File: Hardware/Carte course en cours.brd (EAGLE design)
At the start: 160 x 100 mm, 43 parts, among them J1 AVR_SPI_PROG_3X2NS, J3 PWR IN, J4 RC receiver, J5 ESC, J6 MICRO-SD_CARD_SOCKET, U1 V_REG_317DPACK, U2 ATMEGA328P_TQFP, U3 V_REG_317SMD, U4 FT232RL, U5 TXB0104, U6 MPU6050, Y1 16MHz

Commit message: Place components
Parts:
- removed C13: 100n, rcl:C0805
- removed C14: 2.2n, rcl:C0805
- removed C15: 10n, rcl:C0805
- removed R13: 100k, rcl:R0805
- removed U5: TXB0104, SparkFun-IC-Comms:TSSOP14
- removed U6: MPU6050, invensense:HVQFN24_NS
- added J7: MICRO-SD_CARD_SOCKET, SparkFun-Connectors:MICRO-SD-SOCKET
- added J8: ESC, SparkFun-Connectors:1X02
- C1: value 4.7u -> 22p
- C11: value 100n -> 2.2n
- C12: value 100n -> 10n
- C3: value 22p -> 100n
- C4: value 1u -> 100n
- C6: value 100n -> 4.7u
- C8: value 4.7u -> 100n
- J1: value AVR_SPI_PROG_3X2NS -> (none); device SparkFun-Connectors:2X3-NS -> SparkFun-Connectors:USB-B-MICRO-SMD
- J2: value (none) -> AVR_SPI_PROG_3X2NS; device SparkFun-Connectors:USB-B-MICRO-SMD -> SparkFun-Connectors:2X3-NS
- J6: value MICRO-SD_CARD_SOCKET -> ESC; device SparkFun-Connectors:MICRO-SD-SOCKET -> SparkFun-Connectors:1X02
- R1: value 3k -> 10k
- R2: value 10k -> 1.6k
- R4: value 1.6k -> 330
- R5: value 1k -> 330
- R6, R7: value 330 -> 100k
- U1: value V_REG_317DPACK -> V_REG_317SMD; device SparkFun-IC-Power:V-REG_DPACK -> SparkFun-IC-Power:SOT223
- U3: value V_REG_317SMD -> FT232RL; device SparkFun-IC-Power:SOT223 -> SparkFun-IC-Comms:SSOP28DB
- U4: value FT232RL -> MPU6050; device SparkFun-IC-Comms:SSOP28DB -> invensense:HVQFN24_NS
- moved J4 103.9 mm to (44.5, 14.0), turned to 90 degrees
- moved R8 96.1 mm to (33.7, 4.45), flipped to the bottom, turned to 270 degrees
- moved C2 94.8 mm to (26.7, 21.6), flipped to the bottom
- moved R9 92.0 mm to (35.6, 4.45), flipped to the bottom, turned to 270 degrees
- moved U2 87.8 mm to (34.3, 13.3), flipped to the bottom, turned to 180 degrees
- moved LED2 81.3 mm to (17.8, 3.17)
- moved C3 80.5 mm to (21.6, 22.2), turned to 270 degrees
- moved LED1 79.9 mm to (21.0, 3.17)
- moved C8 79.3 mm to (23.5, 3.17), turned to 90 degrees
- moved C9 73.0 mm to (16.5, 14.6), flipped to the bottom, turned to 180 degrees
- moved Y1 72.0 mm to (26.7, 17.1), flipped to the bottom, turned to 270 degrees
- moved R12 71.9 mm to (26.7, 22.2), turned to 270 degrees
- moved R10 71.9 mm to (41.3, 9.53), turned to 270 degrees
- moved J5 71.1 mm to (1.91, 17.8), turned to 90 degrees
- moved R2 67.9 mm to (12.7, 22.2), turned to 180 degrees
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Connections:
- removed net N$11: J6.CS, R10.1, U5.13
- removed net N$17: J6.DI, U5.12
- removed net N$19: J6.SCLK, U5.11
- removed net N$20: J6.DO, U5.10
- removed net N$3: R4.2, R5.2, U3.1
- removed net RXFTDI: U2.31, U4.5
- removed net TXFTDI: U2.30, U4.1
- removed net VCC: C1.2, J3.2, U1.3
- new net RX_AVR: R7.2, U2.30, U3.1
- new net RX_ESP: J5.2, R6.1
- new net TX_AVR: R6.2, U2.31, U3.5
- new net TX_ESP: J8.1, R7.1
- net +3V3: now also C3.2, C4.2, C5.2, C6.2, C8.1, C9.1, J2.2, J3.2, J7.VCC, J8.2, LED1.A, LED2.A, R1.2, R10.1, R12.1, R3.1, U1.2, U2.18, U2.4, U2.6, U3.20, U3.4, U4.13; no longer C11.1, C12.1, J6.VCC, R10.2, R13.1, R5.1, U3.2, U5.14, U6.13
- net +5V: now also J1.VBUS, U1.3; no longer C10.1, C4.1, C5.2, C6.2, C8.2, C9.2, J1.2, J2.VBUS, LED1.A, LED2.A, R12.1, R2.2, R3.1, U1.4, U2.18, U2.4, U2.6, U3.3, U4.20, U4.4, U5.1
- net CARDDETECT: now also J7.CD2; no longer J6.CD2
- net CS: now also J7.CS; no longer U5.2
- net ESC_OUT: now also J6.2; no longer J5.2
- net GND: now also C1.2, C3.1, C4.1, C8.2, C9.2, J1.GND, J2.6, J6.1, J7.GND, J7.GND1, J7.GND3, R2.1, U3.18, U3.21, U3.25, U3.26, U3.7, U4.1, U4.11, U4.9; no longer C1.1, C13.2, C14.2, C15.2, C3.2, C4.2, C8.1, C9.1, J1.6, J2.GND, J6.GND, J6.GND1, J6.GND3, R1.1, R4.1, U4.21, U4.25, U4.26, U4.7, U5.7, U6.1, U6.11, U6.18, U6.9
- net INT: now also U4.12; no longer U6.12
- net MISO: now also J2.1, J7.DO; no longer J1.1, U5.5
- net MOSI: now also J2.4, J7.DI; no longer J1.4, U5.3
- net N$1: now also R2.2; no longer R1.2
- net N$10: now also C11.1, U4.20; no longer C14.1, U6.20
- net N$12: now also R4.1, U3.23; no longer R6.1, U4.23
- net N$13: now also R5.1, U3.22; no longer R7.1, U4.22
- net N$14: now also R4.2; no longer R6.2
- net N$15: now also R5.2; no longer R7.2
- net N$16: now also C10.1, U4.10; no longer C13.1, U6.10
- net N$18: now also C12.1, U4.8; no longer C15.1, U6.8
- net N$2: now also J1.D-, U3.16; no longer J2.D-, U4.16
- net N$27: now also J7.RSV1, R10.2; no longer J6.RSV1, R11.2
- net N$28: now also J7.RSV2, R12.2; no longer J6.RSV2, R13.2
- net N$29: now also J7.CD1, R11.2; no longer J6.CD1, R12.2
- net N$5: now also C1.1; no longer C2.1
- net N$6: now also C2.1; no longer C3.1
- net N$7: now also J1.D+, U3.15; no longer J2.D+, U4.15
- net RST: now also J2.5, R1.1; no longer J1.5, R2.1
- net SCK: now also J2.3, J7.SCLK; no longer J1.3, U5.4
- net SCL: now also U4.23; no longer U6.23
- net SDA: now also U4.24; no longer U6.24
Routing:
- net +5V: track 25.6 -> 0.00 mm
- net +3V3: track 10.3 -> 0.00 mm
- net GND: track 7.26 -> 0.00 mm
- net N$1: track 6.10 -> 0.00 mm
- net N$3: track 5.83 -> 0.00 mm
- net VCC: track 3.37 -> 0.00 mm
- added copper zone on layer 1, net GND
- added copper zone on layer 16, net GND
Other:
- board size 160 x 100 mm -> 47 x 28.6 mm

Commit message: Add gitignore
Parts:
- moved J4 2.54 mm to (44.5, 16.5), turned to 270 degrees
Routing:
- net +3V3: track 0.00 -> 164.0 mm, vias 0 -> 2
- net INT: track 0.00 -> 38.0 mm, vias 0 -> 2
- net RST: track 0.00 -> 31.4 mm
- net CS: track 0.00 -> 28.8 mm, vias 0 -> 1
- net SCK: track 0.00 -> 23.9 mm, vias 0 -> 1
- net MISO: track 0.00 -> 23.4 mm, vias 0 -> 1
- net TX_AVR: track 0.00 -> 22.9 mm, vias 0 -> 1
- net SDA: track 0.00 -> 22.4 mm
- net TX_ESP: track 0.00 -> 22.3 mm
- net RX_AVR: track 0.00 -> 21.8 mm, vias 0 -> 1
- net MOSI: track 0.00 -> 21.7 mm, vias 0 -> 1
- net SCL: track 0.00 -> 20.4 mm
- net RX_ESP: track 0.00 -> 18.9 mm
- net ESC_OUT: track 0.00 -> 18.9 mm
- net RC_IN: track 0.00 -> 15.9 mm, vias 0 -> 1
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
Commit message: Route
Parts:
- added J9: (no value), SparkFun-Connectors:1X04
- moved J3 40.1 mm to (44.5, 19.7), turned to 270 degrees
- moved C7 13.6 mm to (13.3, 19.7)
- moved C6 11.4 mm to (3.17, 16.5), turned to 0 degrees
- moved R2 3.18 mm to (10.8, 19.7), turned to 270 degrees
- moved R10 3.18 mm to (41.3, 6.35)
- moved C3 2.62 mm to (21.0, 19.7), turned to 0 degrees
- moved R3 2.54 mm to (8.26, 19.7), turned to 90 degrees
- moved LED2 2.29 mm to (19.7, 4.45), turned to 90 degrees
- moved C2 2.01 mm to (26.0, 19.7)
- moved R6 2.01 mm to (21.0, 22.9)
- moved J4 1.91 mm to (44.5, 14.6)
- moved J6 1.90 mm to (44.5, 9.53)
- moved U1 1.90 mm to (10.2, 13.3)
- moved C12 1.80 mm to (10.8, 7.62), turned to 0 degrees
- moved LED1 1.42 mm to (19.7, 2.54), turned to 270 degrees
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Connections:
- net +5V: now also J9.4
- net GND: now also J9.1
- net N$2: now also J9.3
- net N$7: now also J9.2
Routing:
- net +3V3: track 164.0 -> 108.0 mm
- net CS: track 28.8 -> 8.26 mm
- net RST: track 31.4 -> 18.4 mm
- net N$7: track 10.7 -> 23.7 mm
- net INT: track 38.0 -> 25.2 mm, vias 2 -> 0
- net N$2: track 12.3 -> 24.3 mm
- net TX_AVR: track 22.9 -> 30.5 mm
- net GND: track 8.64 -> 1.39 mm, vias 3 -> 0
- net SCK: track 23.9 -> 29.6 mm, vias 1 -> 0
- net +5V: track 8.77 -> 14.0 mm, vias 0 -> 1
- net MOSI: track 21.7 -> 26.8 mm
- net MISO: track 23.4 -> 26.5 mm, vias 1 -> 0
- net N$6: track 6.50 -> 9.37 mm
- net CARDDETECT: track 4.13 -> 6.74 mm
- net TX_ESP: track 22.3 -> 20.6 mm
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
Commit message: Route
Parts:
- moved C10 0.63 mm to (10.8, 10.2)
- moved R6 0.63 mm to (20.3, 22.9)
- moved R7 0.63 mm to (23.5, 22.9), turned to 0 degrees
- moved R10 0.52 mm to (41.8, 6.22), turned to 90 degrees
- moved R4 0.25 mm to (22.6, 6.99)
- moved R9 0.25 mm to (35.8, 4.45)
- moved C9 0.13 mm to (16.5, 13.2)
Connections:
- net +3V3: no longer J2.2
- net +5V: now also J2.2
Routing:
- net +3V3: track 108.0 -> 156.7 mm, vias 2 -> 4
- net +5V: track 14.0 -> 46.4 mm, vias 1 -> 2
- net GND: track 1.39 -> 11.8 mm, vias 0 -> 6
- net TX_ESP: track 20.6 -> 18.6 mm
- net RX_AVR: track 23.3 -> 24.5 mm
- net TX_AVR: track 30.5 -> 31.4 mm
- net RX_ESP: track 20.0 -> 19.3 mm
- net INT: track 25.2 -> 25.7 mm
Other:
- board text added: "5V"
- board text added: "D+"
- board text added: "D-"
- board text added: "GD"
- board text added: "Heol Fief & Dylan Gageot"

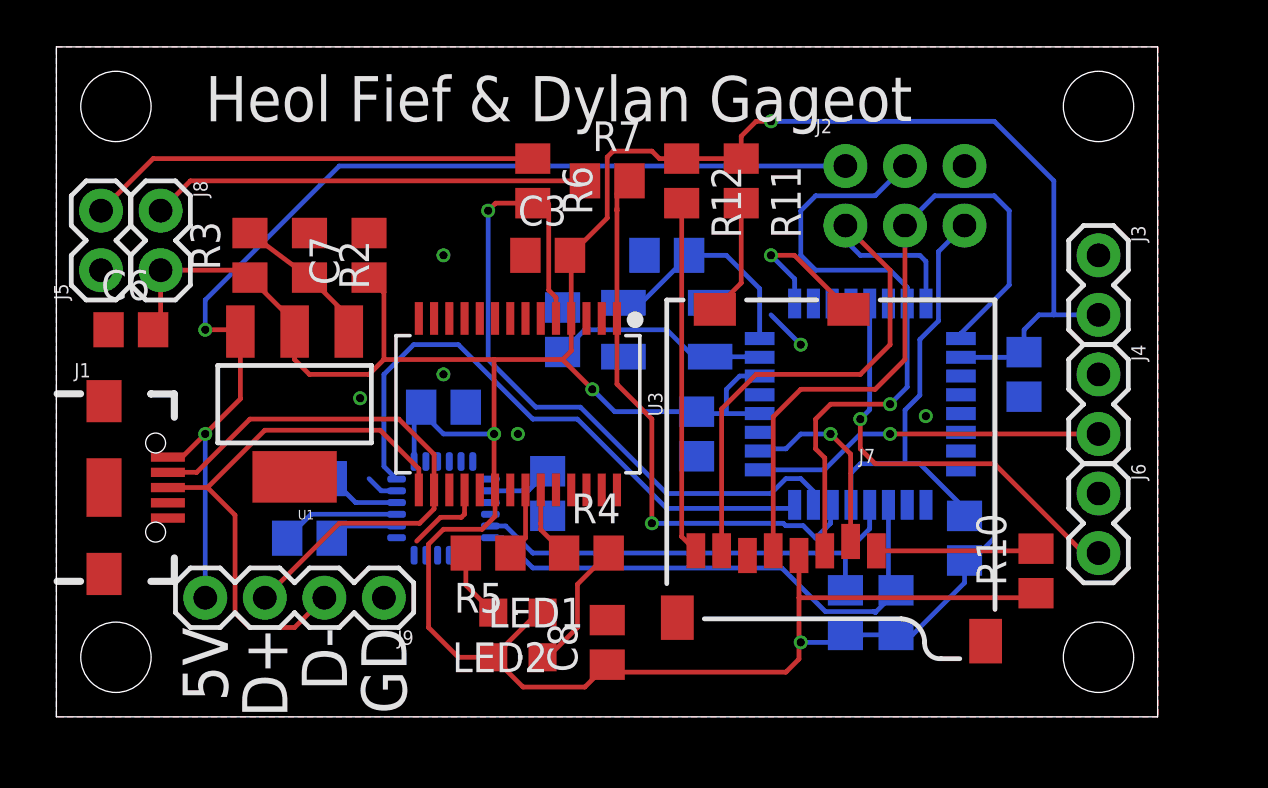
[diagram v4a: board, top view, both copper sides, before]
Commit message: Add silkscreen
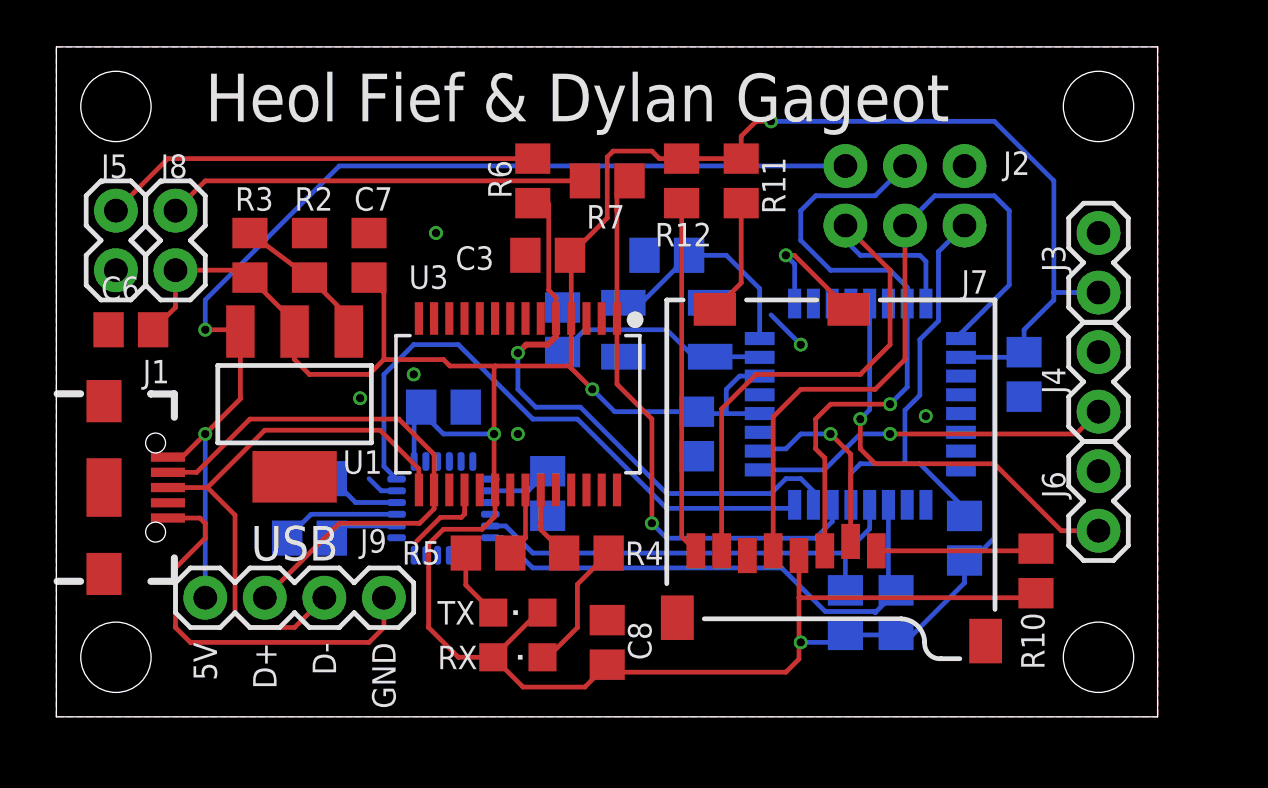
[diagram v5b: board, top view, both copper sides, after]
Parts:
- added LOGO1: OSHW-LOGOM, SparkFun-Aesthetics:OSHW-LOGO-M
- R1: value 10k -> 100k
- moved J3 0.95 mm to (44.5, 20.6)
- moved J4 0.95 mm to (44.5, 15.6)
- moved J6 0.95 mm to (44.5, 10.5)
- moved J5 0.64 mm to (2.54, 19.1)
- moved J8 0.63 mm to (5.08, 21.6)
- renumbered LED1 to RX, LED2 to TX
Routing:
- net GND: track 11.8 -> 29.2 mm
- net TX_AVR: track 31.4 -> 25.4 mm
- net CARDDETECT: track 6.74 -> 5.84 mm
- net +3V3: track 156.7 -> 155.9 mm
- net TX_ESP: track 18.6 -> 18.0 mm
- net RX_ESP: track 19.3 -> 18.7 mm
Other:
- board text added: ">CREVISION"
- board text added: "COURSE EN COURS"
- board text added: "GND"
- board text added: "GPL"
- board text added: "GRAND PRIX DES COLLEGES ET LYCEES"
- board text added: "Rev :"
- board text added: "USB"
- board text removed: "GD"

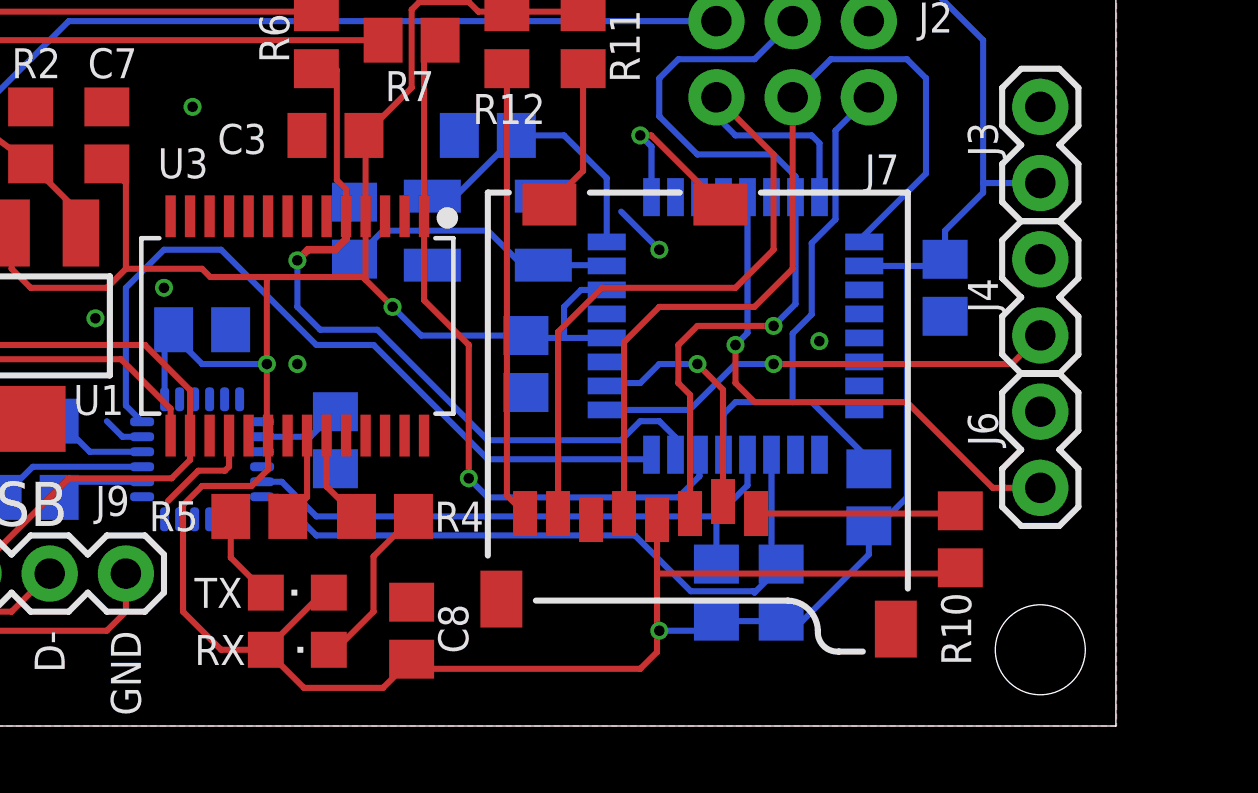
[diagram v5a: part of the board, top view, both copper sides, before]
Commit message: Improce pwr trace lenght
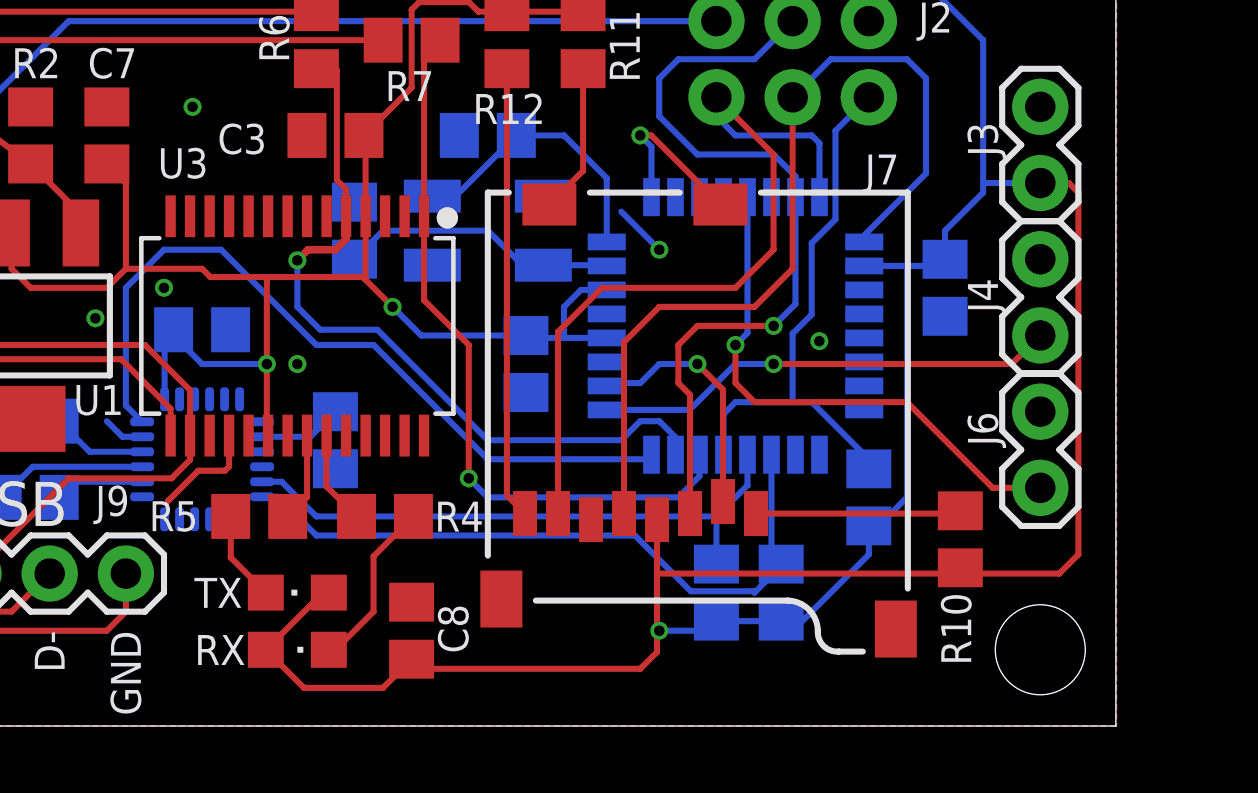
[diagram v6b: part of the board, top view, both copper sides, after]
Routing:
- net +3V3: track 155.9 -> 162.5 mm
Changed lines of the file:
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@@
 <wire x1="29.21" y1="23.81" x2="29.525" y2="23.495" width="0.2032" layer="1"/>
 <wire x1="18.71" y1="9.525" x2="18.71" y2="9.679" width="0.2032" layer="1"/>
-<wire x1="18.71" y1="9.525" x2="18.71" y2="8.55" width="0.2032" layer="1"/>
-<wire x1="18.71" y1="8.55" x2="18.161" y2="8.001" width="0.2032" layer="1"/>
-<wire x1="18.161" y1="8.001" x2="16.51" y2="8.001" width="0.2032" layer="1"/>
-<wire x1="16.51" y1="8.001" x2="15.875" y2="7.366" width="0.2032" layer="1"/>
-<wire x1="15.875" y1="7.366" x2="15.875" y2="3.81" width="0.2032" layer="1"/>
-<wire x1="15.875" y1="3.81" x2="17.145" y2="2.54" width="0.2032" layer="1"/>
-<wire x1="18.635" y1="2.54" x2="17.145" y2="2.54" width="0.2032" layer="1"/>
 <wire x1="18.635" y1="2.54" x2="20.54" y2="4.445" width="0.2032" layer="1"/>
 <wire x1="20.54" y1="4.445" x2="20.735" y2="4.445" width="0.2032" layer="1"/>
@@
 <wire x1="36.515" y1="3.495" x2="35.814" y2="3.495" width="0.2032" layer="16"/>
 <wire x1="38.735" y1="5.715" x2="36.515" y2="3.495" width="0.2032" layer="16"/>
-<wire x1="41.783" y1="5.273" x2="41.59" y2="5.08" width="0.2032" layer="1"/>
+<wire x1="41.75" y1="5.24" x2="41.783" y2="5.273" width="0.2032" layer="1"/>
+<wire x1="41.75" y1="5.24" x2="41.59" y2="5.08" width="0.2032" layer="1"/>
 <wire x1="41.59" y1="5.08" x2="31.675" y2="5.08" width="0.2032" layer="1"/>
 <wire x1="41.275" y1="15.555" x2="41.275" y2="16.51" width="0.2032" layer="16"/>
@@
 <wire x1="18.669" y1="12.065" x2="18.669" y2="14.9011" width="0.2032" layer="1"/>
 <wire x1="18.669" y1="14.9011" x2="18.7325" y2="14.9646" width="0.2032" layer="1"/>
+<wire x1="44.45" y1="18.0975" x2="45.4025" y2="18.0975" width="0.2032" layer="1"/>
+<wire x1="45.4025" y1="18.0975" x2="45.72" y2="17.78" width="0.2032" layer="1"/>
+<wire x1="45.72" y1="17.78" x2="45.72" y2="5.715" width="0.2032" layer="1"/>
+<wire x1="45.72" y1="5.715" x2="45.085" y2="5.08" width="0.2032" layer="1"/>
+<wire x1="45.085" y1="5.08" x2="41.91" y2="5.08" width="0.2032" layer="1"/>
+<wire x1="41.91" y1="5.08" x2="41.75" y2="5.24" width="0.2032" layer="1"/>
 </signal>
 <signal name="RST">
